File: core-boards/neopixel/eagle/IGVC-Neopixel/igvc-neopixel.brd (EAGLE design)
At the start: 50.8 x 50.8 mm, 37 parts, among them IC1 RT8289, IC3 MCP2551T-I/SN, IC4 MEGA8-AI, J1 B2PS-VH(LF)(SN), J4 4-PIN_2MM-H, SW1 SPST_TACT-EVQQ2, X3 16MHz

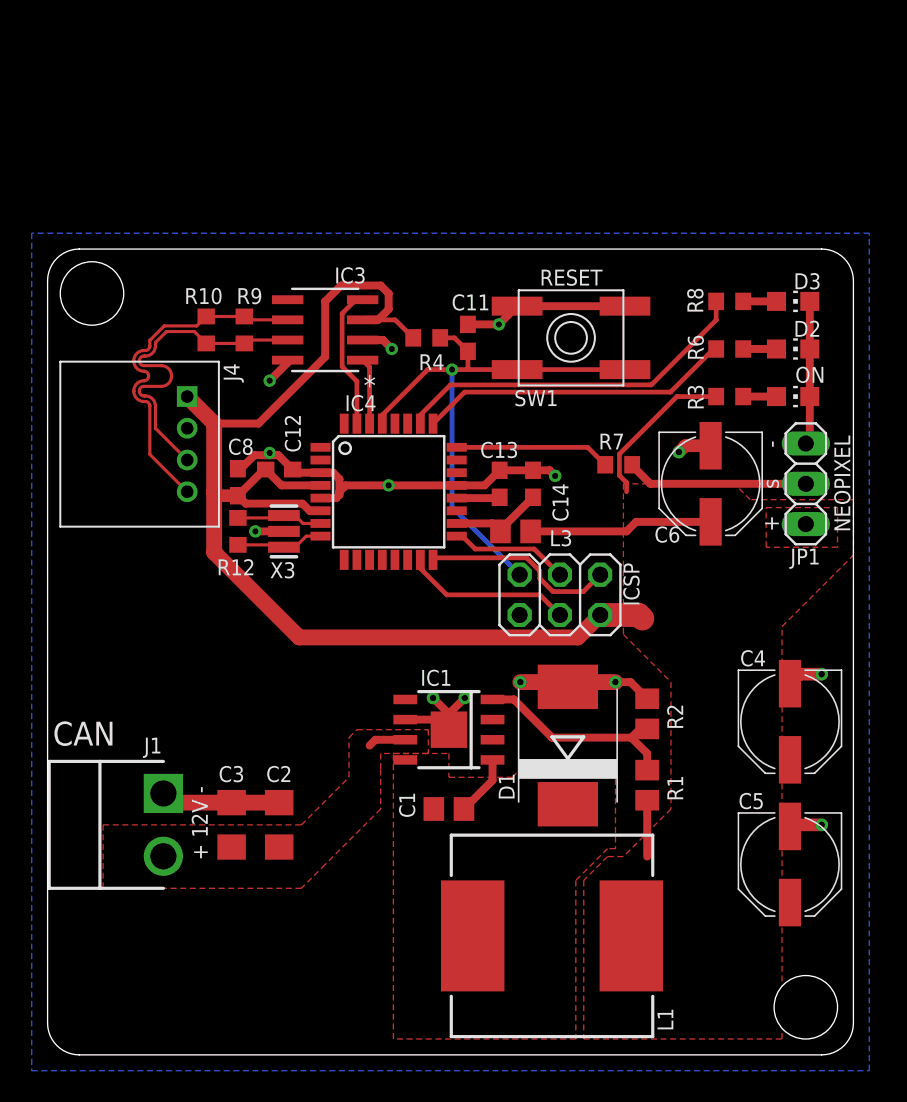
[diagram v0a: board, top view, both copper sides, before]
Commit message: Neopixel: Changes from design review 02/02/2020
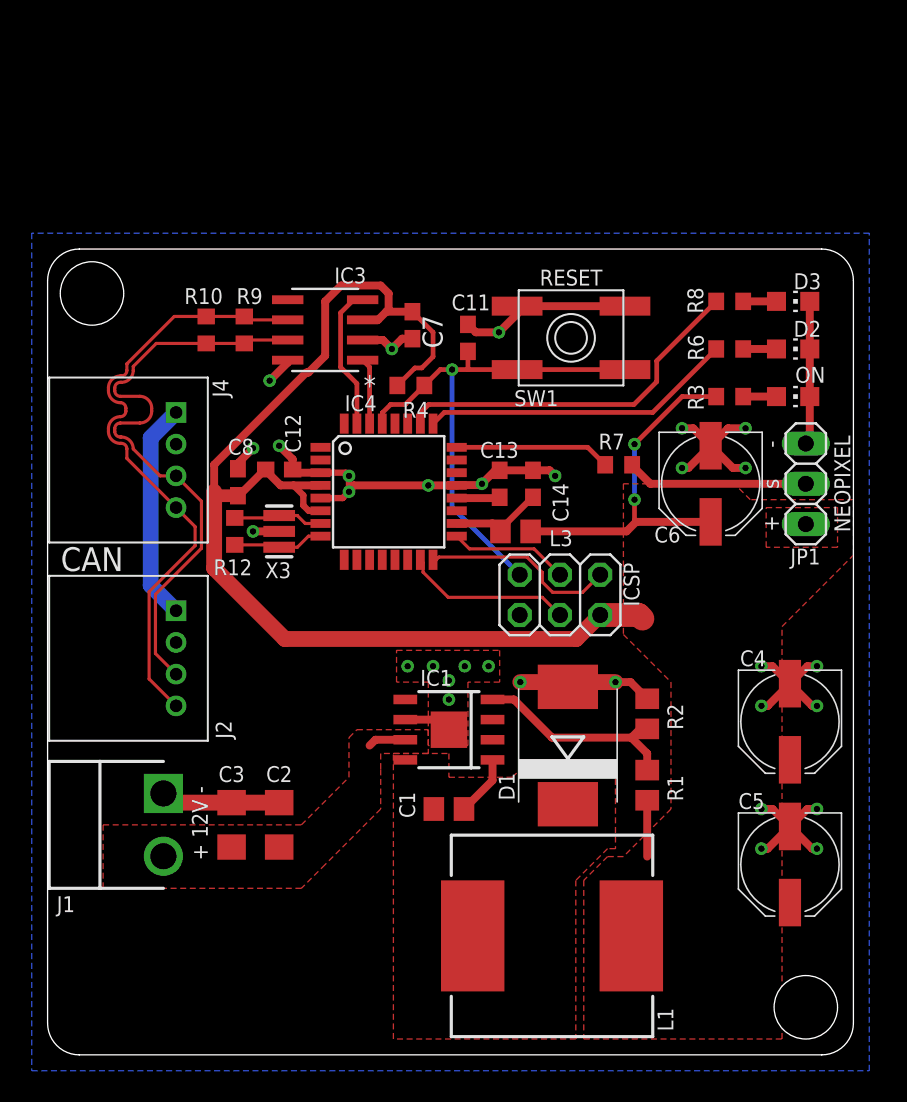
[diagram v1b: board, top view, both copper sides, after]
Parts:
- added C7: 100nF, rcl:C0603
- added J2: 4-PIN_2MM-H, RoboJackets-Connectors:2MM-4-H
- C6: value 1000u -> 1000u 6.3V
- moved R4 3.16 mm to (22.9, 42.2)
- moved J4 1.22 mm to (8.10, 37.5)
- moved X3 0.30 mm to (14.6, 33.0)
- moved R12 0.20 mm to (11.8, 33.0)
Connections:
- net N$1 renamed NEOPIXEL
- new net CAN_5V: J2.1, J4.1
- net +5V: now also C7.1; no longer J4.1
- net CAN_N: now also J2.4
- net CAN_P: now also J2.3
- net GND: now also C7.2, J2.2
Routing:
- net GND: track 78.7 -> 97.7 mm, vias 14 -> 31
- net CAN_P: track 21.1 -> 38.3 mm
- net CAN_N: track 21.6 -> 38.7 mm
- net CAN_5V: track 0.00 -> 13.8 mm
- net !RESET: track 35.0 -> 33.0 mm
- net +5V: track 102.7 -> 102.1 mm, vias 0 -> 2
- added copper zone on layer 1, net GND

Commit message: More design review changes (neopixel)
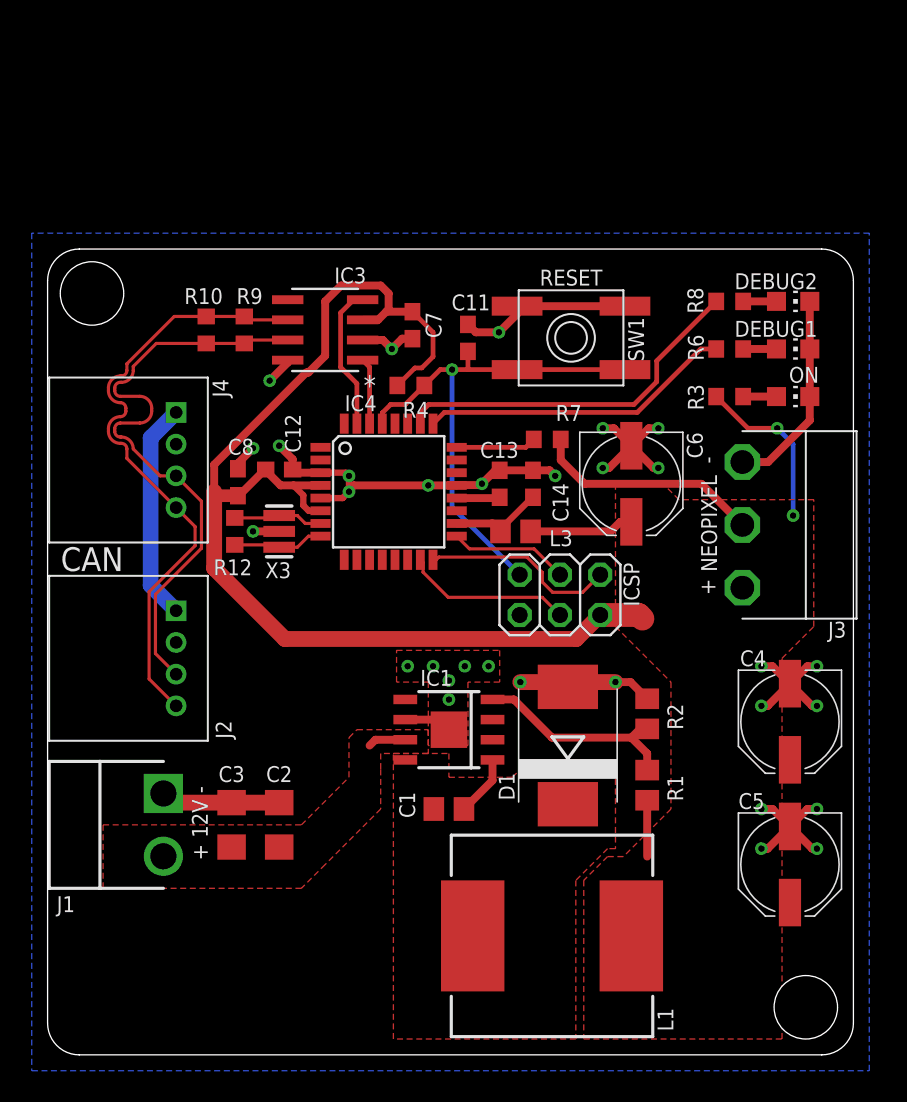
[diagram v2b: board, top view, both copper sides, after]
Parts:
- removed JP1: (no value), pinhead:1X03
- added J3: S3B-VH, IGVC-Connector:S3B-VH
- DEBUG1, DEBUG2: value RED -> BLUE
- moved C6 5.00 mm to (36.8, 36.0)
- moved R7 4.78 mm to (31.5, 38.8)
- renumbered D2 to DEBUG1, D3 to DEBUG2
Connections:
- net +5V: now also J3.1; no longer JP1.1
- net GND: now also J3.3; no longer JP1.3
- net NEOPIXEL: now also J3.2; no longer JP1.2
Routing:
- net +5V: track 102.1 -> 96.9 mm
- net LED_DATA: track 9.81 -> 5.06 mm
- net NEOPIXEL: track 11.5 -> 14.4 mm
- net GND: track 97.7 -> 100.5 mm
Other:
- board text removed: "s"

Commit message: Final changes to neopixel, and BOM
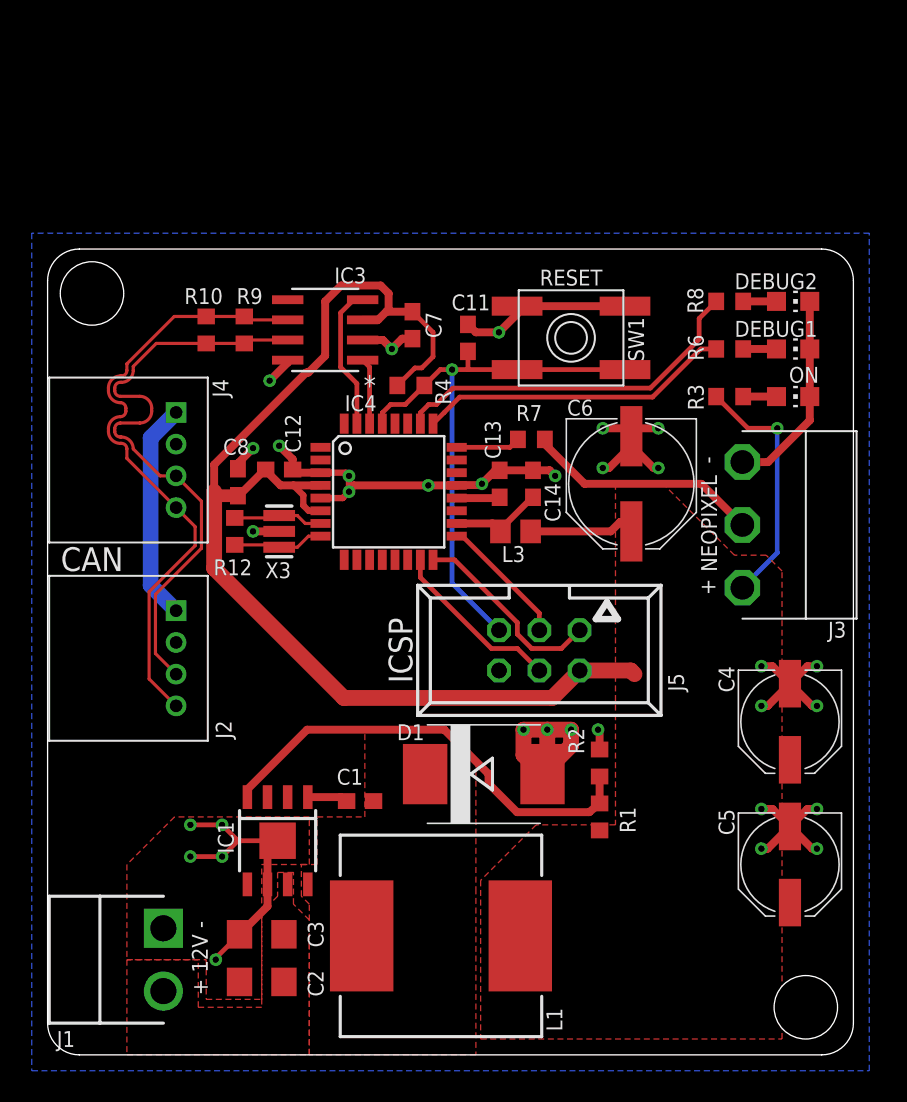
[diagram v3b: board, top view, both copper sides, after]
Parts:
- removed ICSP: ICSP, pinhead:2X03
- added J5: 057-006-1, con-panduit:057-006-1
- C1: value 10n -> 0.01uF; device resistor:C0805 -> resistor:C0603
- C2, C3: value 4.7u -> 4.7uF
- C4, C5: value 47u -> 47uF
- C6: device resistor:PANASONIC_D -> resistor:PANASONIC_E
- C7: value 100nF -> 0.1uF
- DEBUG1, DEBUG2: value BLUE -> YELLOW
- R1, R2: device resistor:R0805 -> resistor:R0603
- moved IC1 12.9 mm to (14.5, 13.5), turned to 180 degrees
- moved C2 9.96 mm to (13.5, 4.60), turned to 180 degrees
- moved J1 8.50 mm to (7.30, 6.00)
- moved C3 7.16 mm to (13.5, 7.60), turned to 180 degrees
- moved L1 7.00 mm to (24.8, 7.50)
- moved C1 5.62 mm to (19.7, 16.0), turned to 0 degrees
- moved D1 5.60 mm to (27.5, 17.7), turned to 0 degrees
- moved R2 4.31 mm to (34.8, 18.4)
- moved R1 3.61 mm to (34.8, 15.0)
- moved R7 1.00 mm to (30.5, 38.8)
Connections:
- net STAT1 renamed DBG1
- net STAT2 renamed DBG2
- net !RESET: now also J5.5; no longer ICSP.5
- net +5V: now also J5.2; no longer ICSP.2
- net GND: now also J5.6; no longer ICSP.6
- net MISO: now also J5.1; no longer ICSP.1
- net MOSI: now also J5.4; no longer ICSP.4
- net SCK: now also J5.3; no longer ICSP.3
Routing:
- net FB: track 13.4 -> 28.7 mm
- net GND: track 100.5 -> 114.8 mm, vias 31 -> 32
- net !RESET: track 33.0 -> 35.9 mm
- net +5V: track 96.9 -> 99.7 mm, vias 2 -> 1
- net +12V: track 2.40 -> 0.00 mm
- net BOOT: track 3.84 -> 2.53 mm
- net LED_DATA: track 5.06 -> 4.06 mm
- net SCK: track 7.51 -> 8.30 mm
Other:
- board text added: "ICSP"
- board text added: "v1.2"
- board text removed: "v1.0"

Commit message: Added CAN Controller to neopixel
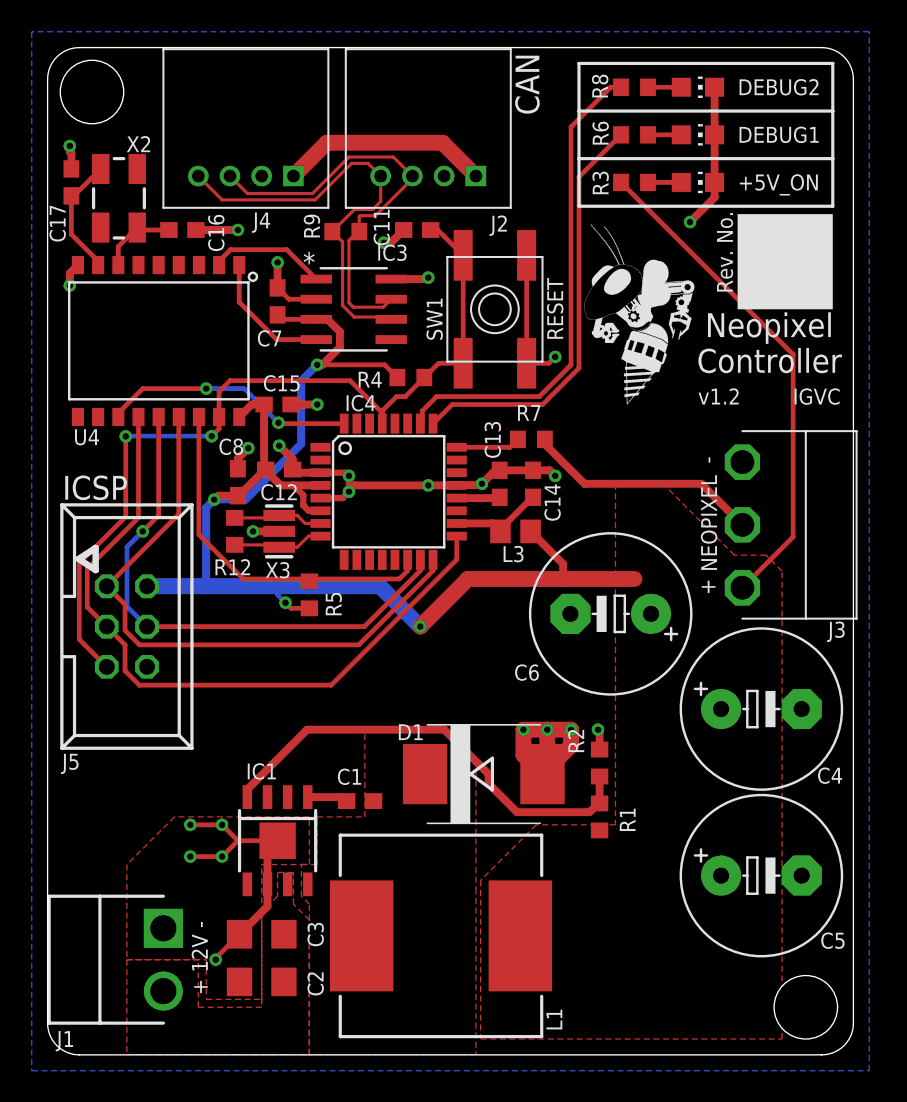
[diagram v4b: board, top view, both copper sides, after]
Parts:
- removed ON: GREEN, led:CHIP-LED0805
- removed R10: 120R, rcl:R0603
- added +5V_ON: GREEN, led:CHIP-LED0805
- added C15: 0.1uF, rcl:C0603
- added C16, C17: 22pF, resistor:C0603
- added R5: 10k, rcl:R0603
- added U4: MCP2515, SparkFun-DigitalIC:SO-18W
- added X2: 16MHz, SparkFun-FreqCtrl:CRYSTAL-SMD-5X3
- C4, C5: device resistor:PANASONIC_D -> resistor:E5-10,5
- C6: device resistor:PANASONIC_E -> resistor:E5-10,5
- R1, R4: value 10K -> 10k
- R2: value 3.16K -> 3.16k
- U$1: value ROBOBUZZ1.0X -> ROBOBUZZ0.6X; device RoboJackets-Aesthetics:ROBOBUZZ_1.0X -> RoboJackets-Aesthetics:ROBOBUZZ_0.6X
- moved U$1 39.6 mm to (36.5, 41.0), flipped to the top
- moved J2 34.3 mm to (24.0, 55.4), turned to 180 degrees
- moved J5 26.0 mm to (5.00, 27.0), turned to 270 degrees
- moved J4 18.4 mm to (12.5, 55.4), turned to 180 degrees
- moved DEBUG1 14.8 mm to (41.0, 58.0)
- moved DEBUG2 14.8 mm to (41.0, 61.0)
- moved R3 14.8 mm to (37.0, 55.0)
- moved R6 14.8 mm to (37.0, 58.0)
- moved R8 14.8 mm to (37.0, 61.0)
- moved R9 8.91 mm to (18.8, 51.9), turned to 0 degrees
- moved C7 8.63 mm to (14.5, 47.5), turned to 90 degrees
- moved C6 8.30 mm to (35.5, 27.8), turned to 180 degrees
- moved C11 7.52 mm to (23.3, 52.0), turned to 0 degrees
- moved SW1 5.13 mm to (28.2, 47.0), turned to 90 degrees
- moved IC3 2.22 mm to (19.3, 47.0), turned to 0 degrees
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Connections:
- net XTAL5 renamed XTAL1
- net XTAL6 renamed XTAL2
- removed net MBED_CAN_RD/1.5C: IC3.1, IC4.30
- removed net MBED_CAN_TD/1.5C: IC3.4, IC4.31
- new net CAN_CS: IC4.14, R5.1, U4.16
- new net CAN_INT: IC4.32, U4.12
- new net CAN_RXD: IC3.1, U4.2
- new net CAN_TXD: IC3.4, U4.1
- new net N$17: C17.2, U4.8, X2.3
- new net N$18: C16.2, U4.7, X2.1
- net !RESET: now also U4.17
- net +5V: now also C15.1, R5.2, U4.18
- net CAN_N: no longer R10.1
- net CAN_P: no longer R10.2
- net GND: now also +5V_ON.C, C15.2, C16.1, C17.1, U4.9; no longer ON.C
- net MISO: now also U4.15
- net MOSI: now also U4.14
- net PWR_LED: now also +5V_ON.A; no longer ON.A
- net SCK: now also U4.13
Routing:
- net SCK: track 8.30 -> 44.4 mm
- net MISO: track 12.5 -> 38.2 mm
- net GND: track 114.8 -> 91.5 mm, vias 32 -> 26
- net MOSI: track 11.0 -> 33.9 mm, vias 0 -> 1
- net CAN_CS: track 0.00 -> 22.8 mm
- net +5V: track 99.7 -> 118.5 mm, vias 1 -> 4
- net !RESET: track 35.9 -> 53.6 mm, vias 1 -> 2
- net CAN_INT: track 0.00 -> 16.0 mm, vias 0 -> 2
- net CAN_P: track 38.3 -> 26.7 mm
- net CAN_N: track 38.7 -> 27.2 mm
- net MBED_CAN_TD/1.5C: track 9.15 -> 0.00 mm
- net CAN_TXD: track 0.00 -> 8.17 mm
- net N$17: track 0.00 -> 7.62 mm
- net DBG2: track 23.0 -> 30.6 mm
- net CAN_RXD: track 0.00 -> 7.44 mm
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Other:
- board size 50.8 x 50.8 mm -> 50.8 x 63.5 mm
